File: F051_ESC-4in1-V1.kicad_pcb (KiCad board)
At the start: 4 copper layers, 46 x 40 mm, 249 parts, among them J1 Conn_01x02, J10 Conn_01x03, J11 Conn_01x03, J12 Conn_01x04, J13 Conn_01x03, J14 Conn_01x03, J15 Conn_01x04, J16 Conn_01x03, J17 Conn_01x03, J2 Conn_01x10, J3 Conn_01x04, J4 Conn_01x03, J5 Conn_01x04, J6 Conn_01x03, J7 Conn_01x03, J8 Conn_01x03, J9 Conn_01x04, Q1 TPHR8504PL, Q10 TPHR8504PL, Q11 TPHR8504PL, Q12 TPHR8504PL, Q13 TPHR8504PL, Q14 TPHR8504PL, Q15 TPHR8504PL, Q16 TPHR8504PL, Q17 TPHR8504PL, Q18 TPHR8504PL, Q19 TPHR8504PL, Q2 TPHR8504PL, Q20 TPHR8504PL, Q21 TPHR8504PL, Q22 TPHR8504PL, Q23 TPHR8504PL, Q24 TPHR8504PL, Q25 TPHR8504PL, Q26 TPHR8504PL, Q27 TPHR8504PL, Q28 TPHR8504PL, Q29 TPHR8504PL, Q3 TPHR8504PL, Q30 TPHR8504PL, Q4 TPHR8504PL, Q5 TPHR8504PL, Q6 TPHR8504PL, Q7 TPHR8504PL, Q8 TPHR8504PL, Q9 TPHR8504PL, U1 FD6288Q, U10 STM32F051K6Ux, U11 FD6288Q, U12 STM32F051K6Ux, U13 FD6288Q, U14 STM32F051K6Ux, U2 STM32F051K6Ux, U3 L78L12_SOT89, U4 LP2985-3.3, U5 INA139, U6 FD6288Q, U7 OPA340NA, U8 STM32F051K6Ux, U9 FD6288Q

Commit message: More design changes
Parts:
- removed C68, C74, C75, C76: 0.1uF, Capacitor_SMD:C_0402_1005Metric
- removed C69, C70, C71: 0.1uF, Capacitor_SMD:C_0603_1608Metric
- removed C72: 10nF, Capacitor_SMD:C_0402_1005Metric
- removed C73: 1uF, Capacitor_SMD:C_0402_1005Metric
- removed D13, D14, D15: 250V, Diode_SMD:D_SOD-523
- removed FB5: 100@100MHz, Inductor_SMD:L_0603_1608Metric
- removed J15: Conn_01x04, Connector_PinHeader_2.54mm:PinHeader_1x04_P2.54mm_Vertical
- removed J16: Conn_01x03, Connector_PinHeader_2.54mm:PinHeader_1x03_P2.54mm_Vertical
- removed J17: Conn_01x03, Connector_Wire:Conn_MotorPhase
- removed Q25, Q26, Q27, Q28, Q29, Q30: TPHR8504PL, Footprints:TPHR8504PL
- removed R72, R73, R74, R75, R76, R77: 10, Resistor_SMD:R_0402_1005Metric
- removed R78, R79, R80, R81, R83, R84: 10k, Resistor_SMD:R_0402_1005Metric
- removed R82, R85, R86, R87, R88: 1k, Resistor_SMD:R_0402_1005Metric
- removed U13: FD6288Q, Package_DFN_QFN:QFN-24-1EP_4x4mm_P0.5mm_EP2.7x2.7mm
- removed U14: STM32F051K6Ux, Package_DFN_QFN:QFN-32-1EP_5x5mm_P0.5mm_EP3.45x3.45mm
- C1, C32, C41: value 0.1uF -> 10nF
- C12, C34, C35, C43, C44: footprint Capacitor_SMD:C_0603_1608Metric -> Capacitor_SMD:C_0402_1005Metric
- C15, C38, C39, C40, C47, C48, C49: footprint Capacitor_SMD:C_0402_1005Metric -> Capacitor_SMD:C_0603_1608Metric
- C2: value 0.1uF -> 1uF
- C3, C36, C45: value 10nF -> 0.1uF
- C33, C42: value 0.1uF -> 1uF; footprint Capacitor_SMD:C_0603_1608Metric -> Capacitor_SMD:C_0402_1005Metric
- C37, C46, C6: value 1uF -> 0.1uF
- J10, J11, J12, J13, J14, J9, Q2, Q20: moved to B.Cu
- J4: footprint Connector_Wire:Conn_MotorPhase -> Connector_PinHeader_2.54mm:PinHeader_1x03_P2.54mm_Vertical
- J6: footprint Connector_PinHeader_2.54mm:PinHeader_1x03_P2.54mm_Vertical -> Connector_Wire:Conn_MotorPhase
- Q24, Q6: moved to F.Cu
- R10, R12, R38, R39, R40, R41, R43, R55, R56, R57, R58, R60, R7, R8, R9: value 10 -> 10k
- R11, R42, R59: value 10 -> 1k
- R14, R15, R17, R45, R46, R47, R62, R63, R64: value 10k -> 1k
- R18, R19, R49, R50, R66, R67: value 10k -> 10
- R20, R21, R23, R24, R51, R52, R53, R54, R68, R69, R70, R71: value 1k -> 10
- U1, U11, U9: value FD6288Q -> STM32F051K6Ux; footprint Package_DFN_QFN:QFN-24-1EP_4x4mm_P0.5mm_EP2.7x2.7mm -> Package_DFN_QFN:QFN-32-1EP_5x5mm_P0.5mm_EP3.45x3.45mm
- U10, U12, U2: value STM32F051K6Ux -> FD6288Q; footprint Package_DFN_QFN:QFN-32-1EP_5x5mm_P0.5mm_EP3.45x3.45mm -> Package_DFN_QFN:QFN-24-1EP_4x4mm_P0.5mm_EP2.7x2.7mm
- moved Q6 233.4 mm to (-8.07, 40.9), turned to 0 degrees
- moved Q18 231.0 mm to (-25.7, 28.0)
- moved Q13 221.5 mm to (-18.0, 27.2), turned to 180 degrees
- moved Q15 217.0 mm to (-18.0, 32.8), turned to 180 degrees
- moved Q17 213.0 mm to (-18.0, 38.4), turned to 180 degrees
- moved Q1 151.8 mm to (-0.31, 40.1), turned to 180 degrees
- moved Q3 146.2 mm to (-0.31, 45.7), turned to 180 degrees
- moved Q5 141.3 mm to (-0.31, 51.4), turned to 180 degrees
- moved Q24 115.9 mm to (148.8, 121.1), turned to 180 degrees
- moved R30 101.3 mm to (140.8, 53.3), turned to 0 degrees
- moved R31 101.3 mm to (140.8, 52.4), turned to 0 degrees
- moved R28 100.4 mm to (140.8, 56.3), turned to 0 degrees
- moved R29 100.1 mm to (140.8, 54.3), turned to 0 degrees
- moved R27 99.3 mm to (140.8, 57.3), turned to 0 degrees
- moved R35 98.9 mm to (140.8, 55.3), turned to 180 degrees
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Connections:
- C1 pad 1: +3V3 -> +3.3VA
- C11 pad 1: +12V -> /MCU 1/NRST
- C12 pad 1: /MOSFET Driver 1/VB2 -> +12V
- C12 pad 2: /MCU 1/PhaseB -> GND
- C14 pad 1: /MOSFET Driver 1/VB3 -> /MOSFET Driver 1/VB2
- C14 pad 2: /MCU 1/PhaseC -> /MCU 1/PhaseB
- C15 pad 1: /MCU 1/NRST -> /MOSFET Driver 1/VB3
- C15 pad 2: GND -> /MCU 1/PhaseC
- C2 pad 1: +3V3 -> +3.3VA
- C3 pad 1: +3.3VA -> +3V3
- C32 pad 1: +12V -> +3.3VA
- C33 pad 1: /MOSFET Driver 3/VB1 -> +3.3VA
- C33 pad 2: /MCU 3/PhaseA -> GND
- C34 pad 1: /MOSFET Driver 3/VB2 -> +3V3
- C34 pad 2: /MCU 3/PhaseB -> GND
- C35 pad 1: /MOSFET Driver 3/VB3 -> +3V3
- C35 pad 2: /MCU 3/PhaseC -> GND
- C36 pad 1: +3.3VA -> /MCU 3/NRST
- C37 pad 1: +3.3VA -> +12V
- C38 pad 1: +3V3 -> /MOSFET Driver 3/VB1
- C38 pad 2: GND -> /MCU 3/PhaseA
- C39 pad 1: +3V3 -> /MOSFET Driver 3/VB2
- C39 pad 2: GND -> /MCU 3/PhaseB
- C40 pad 1: /MCU 3/NRST -> /MOSFET Driver 3/VB3
- C40 pad 2: GND -> /MCU 3/PhaseC
- C41 pad 1: +12V -> +3.3VA
- C42 pad 1: /MOSFET Driver 4/VB1 -> +3.3VA
- C42 pad 2: /MCU 4/PhaseA -> GND
- C43 pad 1: /MOSFET Driver 4/VB2 -> +3V3
- C43 pad 2: /MCU 4/PhaseB -> GND
- C44 pad 1: /MOSFET Driver 4/VB3 -> +3V3
- C44 pad 2: /MCU 4/PhaseC -> GND
- C45 pad 1: +3.3VA -> /MCU 4/NRST
- C46 pad 1: +3.3VA -> +12V
- C47 pad 1: +3V3 -> /MOSFET Driver 4/VB1
- C47 pad 2: GND -> /MCU 4/PhaseA
- C48 pad 1: +3V3 -> /MOSFET Driver 4/VB2
- C48 pad 2: GND -> /MCU 4/PhaseB
- C49 pad 1: /MCU 4/NRST -> /MOSFET Driver 4/VB3
- C49 pad 2: GND -> /MCU 4/PhaseC
- C6 pad 1: +3.3VA -> +3V3
- D2 pad 1: /MOSFET Driver 1/VB2 -> /MOSFET Driver 1/VB1
- D3 pad 1: /MOSFET Driver 1/VB1 -> /MOSFET Driver 1/VB2
- J2 pad 10: /PWM_4 -> (no net)
- J2 pad 9: /PWM_3 -> (no net)
- J4 pad 1: /MCU 1/PhaseC -> /MCU 1/NRST
- J4 pad 2: /MCU 1/PhaseB -> /MCU 1/USART1_RX
- J4 pad 3: /MCU 1/PhaseA -> /MCU 1/USART1_TX
- J6 pad 1: /MCU 1/NRST -> /MCU 1/PhaseC
- J6 pad 2: /MCU 1/USART1_RX -> /MCU 1/PhaseB
- J6 pad 3: /MCU 1/USART1_TX -> /MCU 1/PhaseA
- R10 pad 1: Net-(Q4-Pad4) -> /MCU 1/SenseB
- R10 pad 2: /MOSFET Driver 1/LO2 -> /MCU 1/SenseCOM
- R11 pad 1: Net-(Q5-Pad4) -> Net-(R11-Pad1)
- R11 pad 2: /MOSFET Driver 1/HO3 -> /PWM_1
- R12 pad 1: Net-(Q6-Pad4) -> /MCU 1/SenseC
- R12 pad 2: /MOSFET Driver 1/LO3 -> /MCU 1/PhaseC
- R13 pad 1: /MCU 1/SenseA -> /MCU 1/SenseC
- R13 pad 2: /MCU 1/PhaseA -> /MCU 1/SenseCOM
- R14 pad 1: /MCU 1/SenseA -> GND
- R14 pad 2: /MCU 1/SenseCOM -> /MCU 1/SenseA
- R15 pad 1: /MCU 1/SenseB -> GND
- R15 pad 2: /MCU 1/PhaseB -> /MCU 1/SenseB
- R16 pad 2: /MCU 1/SenseA -> /MCU 1/SenseC
- R17 pad 1: /MCU 1/SenseB -> /MCU 1/BOOT0
- R17 pad 2: /MCU 1/SenseCOM -> GND
- R18 pad 1: /MCU 1/SenseC -> Net-(Q1-Pad4)
- R18 pad 2: /MCU 1/PhaseC -> /MOSFET Driver 1/HO1
- R19 pad 1: /MCU 1/SenseC -> Net-(Q2-Pad4)
- R19 pad 2: /MCU 1/SenseCOM -> /MOSFET Driver 1/LO1
- R20 pad 1: GND -> Net-(Q3-Pad4)
- R20 pad 2: /MCU 1/SenseB -> /MOSFET Driver 1/HO2
- R21 pad 1: GND -> Net-(Q4-Pad4)
- R21 pad 2: /MCU 1/SenseC -> /MOSFET Driver 1/LO2
- R23 pad 1: /MCU 1/BOOT0 -> Net-(Q5-Pad4)
- R23 pad 2: GND -> /MOSFET Driver 1/HO3
- R24 pad 1: Net-(R24-Pad1) -> Net-(Q6-Pad4)
- R24 pad 2: /PWM_1 -> /MOSFET Driver 1/LO3
- R38 pad 1: Net-(Q13-Pad4) -> /MCU 3/SenseA
- R38 pad 2: /MOSFET Driver 3/HO1 -> /MCU 3/PhaseA
- R39 pad 1: Net-(Q14-Pad4) -> /MCU 3/SenseA
- R39 pad 2: /MOSFET Driver 3/LO1 -> /MCU 3/SenseCOM
- R40 pad 1: Net-(Q15-Pad4) -> /MCU 3/SenseB
- R40 pad 2: /MOSFET Driver 3/HO2 -> /MCU 3/PhaseB
- R41 pad 1: Net-(Q16-Pad4) -> /MCU 3/SenseB
- R41 pad 2: /MOSFET Driver 3/LO2 -> /MCU 3/SenseCOM
- R42 pad 1: Net-(Q17-Pad4) -> Net-(R42-Pad1)
- R42 pad 2: /MOSFET Driver 3/HO3 -> /PWM_2
- R43 pad 1: Net-(Q18-Pad4) -> /MCU 3/SenseC
- R43 pad 2: /MOSFET Driver 3/LO3 -> /MCU 3/PhaseC
- R44 pad 1: /MCU 3/SenseA -> /MCU 3/SenseC
- R44 pad 2: /MCU 3/PhaseA -> /MCU 3/SenseCOM
- R45 pad 1: /MCU 3/SenseA -> GND
- R45 pad 2: /MCU 3/SenseCOM -> /MCU 3/SenseA
- R46 pad 1: /MCU 3/SenseB -> GND
- R46 pad 2: /MCU 3/PhaseB -> /MCU 3/SenseB
- R47 pad 1: /MCU 3/SenseB -> GND
- R47 pad 2: /MCU 3/SenseCOM -> /MCU 3/SenseC
- R48 pad 1: Net-(R48-Pad1) -> /MCU 3/BOOT0
- R48 pad 2: /PWM_3 -> GND
- R49 pad 1: /MCU 3/SenseC -> Net-(Q13-Pad4)
- R49 pad 2: /MCU 3/PhaseC -> /MOSFET Driver 3/HO1
- R50 pad 1: /MCU 3/SenseC -> Net-(Q14-Pad4)
- R50 pad 2: /MCU 3/SenseCOM -> /MOSFET Driver 3/LO1
- R51 pad 1: GND -> Net-(Q15-Pad4)
- R51 pad 2: /MCU 3/SenseA -> /MOSFET Driver 3/HO2
- R52 pad 1: GND -> Net-(Q16-Pad4)
- R52 pad 2: /MCU 3/SenseB -> /MOSFET Driver 3/LO2
- R53 pad 1: GND -> Net-(Q17-Pad4)
- R53 pad 2: /MCU 3/SenseC -> /MOSFET Driver 3/HO3
- R54 pad 1: /MCU 3/BOOT0 -> Net-(Q18-Pad4)
- R54 pad 2: GND -> /MOSFET Driver 3/LO3
- R55 pad 1: Net-(Q19-Pad4) -> /MCU 4/SenseA
- R55 pad 2: /MOSFET Driver 4/HO1 -> /MCU 4/PhaseA
- R56 pad 1: Net-(Q20-Pad4) -> /MCU 4/SenseA
- R56 pad 2: /MOSFET Driver 4/LO1 -> /MCU 4/SenseCOM
- R57 pad 1: Net-(Q21-Pad4) -> /MCU 4/SenseB
- R57 pad 2: /MOSFET Driver 4/HO2 -> /MCU 4/PhaseB
- R58 pad 1: Net-(Q22-Pad4) -> /MCU 4/SenseB
- R58 pad 2: /MOSFET Driver 4/LO2 -> /MCU 4/SenseCOM
- R59 pad 1: Net-(Q23-Pad4) -> Net-(R59-Pad1)
- R59 pad 2: /MOSFET Driver 4/HO3 -> /PWM_2
- R60 pad 1: Net-(Q24-Pad4) -> /MCU 4/SenseC
- R60 pad 2: /MOSFET Driver 4/LO3 -> /MCU 4/PhaseC
- R61 pad 1: /MCU 4/SenseA -> /MCU 4/SenseC
- R61 pad 2: /MCU 4/PhaseA -> /MCU 4/SenseCOM
- R62 pad 1: /MCU 4/SenseA -> GND
- R62 pad 2: /MCU 4/SenseCOM -> /MCU 4/SenseA
- R63 pad 1: /MCU 4/SenseB -> GND
- R63 pad 2: /MCU 4/PhaseB -> /MCU 4/SenseB
- R64 pad 1: /MCU 4/SenseB -> GND
- R64 pad 2: /MCU 4/SenseCOM -> /MCU 4/SenseC
- R65 pad 1: Net-(R65-Pad1) -> /MCU 4/BOOT0
- R65 pad 2: /PWM_4 -> GND
- R66 pad 1: /MCU 4/SenseC -> Net-(Q19-Pad4)
- R66 pad 2: /MCU 4/PhaseC -> /MOSFET Driver 4/HO1
- R67 pad 1: /MCU 4/SenseC -> Net-(Q20-Pad4)
- R67 pad 2: /MCU 4/SenseCOM -> /MOSFET Driver 4/LO1
- R68 pad 1: GND -> Net-(Q21-Pad4)
- R68 pad 2: /MCU 4/SenseA -> /MOSFET Driver 4/HO2
- R69 pad 1: GND -> Net-(Q22-Pad4)
- R69 pad 2: /MCU 4/SenseB -> /MOSFET Driver 4/LO2
- R7 pad 1: Net-(Q1-Pad4) -> /MCU 1/SenseA
- R7 pad 2: /MOSFET Driver 1/HO1 -> /MCU 1/PhaseA
- R70 pad 1: GND -> Net-(Q23-Pad4)
- R70 pad 2: /MCU 4/SenseC -> /MOSFET Driver 4/HO3
- R71 pad 1: /MCU 4/BOOT0 -> Net-(Q24-Pad4)
- R71 pad 2: GND -> /MOSFET Driver 4/LO3
- R8 pad 1: Net-(Q2-Pad4) -> /MCU 1/SenseA
- R8 pad 2: /MOSFET Driver 1/LO1 -> /MCU 1/SenseCOM
- R9 pad 1: Net-(Q3-Pad4) -> /MCU 1/SenseB
- R9 pad 2: /MOSFET Driver 1/HO2 -> /MCU 1/PhaseB
- U1 pad 1: /MCU 1/LIN1 -> +3V3
- U1 pad 10: /MOSFET Driver 1/LO2 -> /MCU 1/SenseB
- U1 pad 11: /MOSFET Driver 1/LO1 -> /MCU 1/SenseA
- U1 pad 12: /MCU 1/PhaseC -> (no net)
- U1 pad 13: /MOSFET Driver 1/HO3 -> /MCU 1/LIN3
- U1 pad 14: /MOSFET Driver 1/VB3 -> /MCU 1/LIN2
- U1 pad 15: /MCU 1/PhaseB -> /MCU 1/LIN1
- U1 pad 16: /MOSFET Driver 1/HO2 -> (no net)
- U1 pad 17: /MOSFET Driver 1/VB2 -> +3V3
- U1 pad 18: /MCU 1/PhaseA -> /MCU 1/HIN1
- U1 pad 19: /MOSFET Driver 1/HO1 -> /MCU 1/HIN2
- U1 pad 2: /MCU 1/LIN2 -> (no net)
- U1 pad 20: /MOSFET Driver 1/VB1 -> /MOSFET Driver 1/HIN1
- U1 pad 22: /MOSFET Driver 1/HIN1 -> (no net)
- U1 pad 23: /MCU 1/HIN2 -> /MCU 1/SWDIO
- U1 pad 24: /MCU 1/HIN1 -> /MCU 1/SWCLK
- U1 pad 25: GND -> (no net)
- U1 pad 3: /MCU 1/LIN3 -> (no net)
- U1 pad 4: +12V -> /MCU 1/NRST
- U1 pad 5: (no net) -> +3.3VA
- U1 pad 6: GND -> /MCU 1/SenseC
- U1 pad 7: (no net) -> /MCU 1/SenseCOM
- U1 pad 8: (no net) -> Net-(R11-Pad1)
- U1 pad 9: /MOSFET Driver 1/LO3 -> (no net)
- U10 pad 1: +3V3 -> /MCU 3/LIN1
- U10 pad 10: /MCU 3/SenseB -> /MOSFET Driver 3/LO2
- U10 pad 11: /MCU 3/SenseA -> /MOSFET Driver 3/LO1
- U10 pad 12: (no net) -> /MCU 3/PhaseC
- U10 pad 13: /MCU 3/LIN3 -> /MOSFET Driver 3/HO3
- U10 pad 14: /MCU 3/LIN2 -> /MOSFET Driver 3/VB3
- U10 pad 15: /MCU 3/LIN1 -> /MCU 3/PhaseB
- U10 pad 16: (no net) -> /MOSFET Driver 3/HO2
- U10 pad 17: +3V3 -> /MOSFET Driver 3/VB2
- U10 pad 18: /MCU 3/HIN1 -> /MCU 3/PhaseA
- U10 pad 19: /MCU 3/HIN2 -> /MOSFET Driver 3/HO1
- U10 pad 2: (no net) -> /MCU 3/LIN2
- U10 pad 20: /MOSFET Driver 3/HIN1 -> /MOSFET Driver 3/VB1
- U10 pad 22: (no net) -> /MOSFET Driver 3/HIN1
- U10 pad 23: /MCU 3/SWDIO -> /MCU 3/HIN2
- U10 pad 24: /MCU 3/SWCLK -> /MCU 3/HIN1
- U10 pad 25: (no net) -> GND
- U10 pad 3: (no net) -> /MCU 3/LIN3
- U10 pad 4: /MCU 3/NRST -> +12V
- U10 pad 5: +3.3VA -> (no net)
- U10 pad 6: /MCU 3/SenseC -> GND
- U10 pad 7: /MCU 3/SenseCOM -> (no net)
- U10 pad 8: Net-(R48-Pad1) -> (no net)
- U10 pad 9: (no net) -> /MOSFET Driver 3/LO3
- U11 pad 1: /MCU 4/LIN1 -> +3V3
- U11 pad 10: /MOSFET Driver 4/LO2 -> /MCU 4/SenseB
- U11 pad 11: /MOSFET Driver 4/LO1 -> /MCU 4/SenseA
- U11 pad 12: /MCU 4/PhaseC -> (no net)
- U11 pad 13: /MOSFET Driver 4/HO3 -> /MCU 4/LIN3
- U11 pad 14: /MOSFET Driver 4/VB3 -> /MCU 4/LIN2
- U11 pad 15: /MCU 4/PhaseB -> /MCU 4/LIN1
- U11 pad 16: /MOSFET Driver 4/HO2 -> (no net)
- U11 pad 17: /MOSFET Driver 4/VB2 -> +3V3
- U11 pad 18: /MCU 4/PhaseA -> /MCU 4/HIN1
- U11 pad 19: /MOSFET Driver 4/HO1 -> /MCU 4/HIN2
- U11 pad 2: /MCU 4/LIN2 -> (no net)
- U11 pad 20: /MOSFET Driver 4/VB1 -> /MOSFET Driver 4/HIN1
- U11 pad 22: /MOSFET Driver 4/HIN1 -> (no net)
- U11 pad 23: /MCU 4/HIN2 -> /MCU 4/SWDIO
- U11 pad 24: /MCU 4/HIN1 -> /MCU 4/SWCLK
- U11 pad 25: GND -> (no net)
- U11 pad 3: /MCU 4/LIN3 -> (no net)
- U11 pad 4: +12V -> /MCU 4/NRST
- U11 pad 5: (no net) -> +3.3VA
- U11 pad 6: GND -> /MCU 4/SenseC
- U11 pad 7: (no net) -> /MCU 4/SenseCOM
- U11 pad 8: (no net) -> Net-(R59-Pad1)
- U11 pad 9: /MOSFET Driver 4/LO3 -> (no net)
- U12 pad 1: +3V3 -> /MCU 4/LIN1
- U12 pad 10: /MCU 4/SenseB -> /MOSFET Driver 4/LO2
- U12 pad 11: /MCU 4/SenseA -> /MOSFET Driver 4/LO1
- U12 pad 12: (no net) -> /MCU 4/PhaseC
- U12 pad 13: /MCU 4/LIN3 -> /MOSFET Driver 4/HO3
- U12 pad 14: /MCU 4/LIN2 -> /MOSFET Driver 4/VB3
- U12 pad 15: /MCU 4/LIN1 -> /MCU 4/PhaseB
- U12 pad 16: (no net) -> /MOSFET Driver 4/HO2
- U12 pad 17: +3V3 -> /MOSFET Driver 4/VB2
- U12 pad 18: /MCU 4/HIN1 -> /MCU 4/PhaseA
- U12 pad 19: /MCU 4/HIN2 -> /MOSFET Driver 4/HO1
- U12 pad 2: (no net) -> /MCU 4/LIN2
- U12 pad 20: /MOSFET Driver 4/HIN1 -> /MOSFET Driver 4/VB1
- U12 pad 22: (no net) -> /MOSFET Driver 4/HIN1
- U12 pad 23: /MCU 4/SWDIO -> /MCU 4/HIN2
- U12 pad 24: /MCU 4/SWCLK -> /MCU 4/HIN1
- U12 pad 25: (no net) -> GND
- U12 pad 3: (no net) -> /MCU 4/LIN3
- U12 pad 4: /MCU 4/NRST -> +12V
- U12 pad 5: +3.3VA -> (no net)
- U12 pad 6: /MCU 4/SenseC -> GND
- U12 pad 7: /MCU 4/SenseCOM -> (no net)
- U12 pad 8: Net-(R65-Pad1) -> (no net)
- U12 pad 9: (no net) -> /MOSFET Driver 4/LO3
- U2 pad 1: +3V3 -> /MCU 1/LIN1
- U2 pad 10: /MCU 1/SenseB -> /MOSFET Driver 1/LO2
- U2 pad 11: /MCU 1/SenseA -> /MOSFET Driver 1/LO1
- U2 pad 12: (no net) -> /MCU 1/PhaseC
- U2 pad 13: /MCU 1/LIN3 -> /MOSFET Driver 1/HO3
- U2 pad 14: /MCU 1/LIN2 -> /MOSFET Driver 1/VB3
- U2 pad 15: /MCU 1/LIN1 -> /MCU 1/PhaseB
- U2 pad 16: (no net) -> /MOSFET Driver 1/HO2
- U2 pad 17: +3V3 -> /MOSFET Driver 1/VB2
- U2 pad 18: /MCU 1/HIN1 -> /MCU 1/PhaseA
- U2 pad 19: /MCU 1/HIN2 -> /MOSFET Driver 1/HO1
- U2 pad 2: (no net) -> /MCU 1/LIN2
- U2 pad 20: /MOSFET Driver 1/HIN1 -> /MOSFET Driver 1/VB1
- U2 pad 22: (no net) -> /MOSFET Driver 1/HIN1
- U2 pad 23: /MCU 1/SWDIO -> /MCU 1/HIN2
- U2 pad 24: /MCU 1/SWCLK -> /MCU 1/HIN1
- U2 pad 25: (no net) -> GND
- U2 pad 3: (no net) -> /MCU 1/LIN3
- U2 pad 4: /MCU 1/NRST -> +12V
- U2 pad 5: +3.3VA -> (no net)
- U2 pad 6: /MCU 1/SenseC -> GND
- U2 pad 7: /MCU 1/SenseCOM -> (no net)
- U2 pad 8: Net-(R24-Pad1) -> (no net)
- U2 pad 9: (no net) -> /MOSFET Driver 1/LO3
- U9 pad 1: /MCU 3/LIN1 -> +3V3
- U9 pad 10: /MOSFET Driver 3/LO2 -> /MCU 3/SenseB
- U9 pad 11: /MOSFET Driver 3/LO1 -> /MCU 3/SenseA
- U9 pad 12: /MCU 3/PhaseC -> (no net)
- U9 pad 13: /MOSFET Driver 3/HO3 -> /MCU 3/LIN3
- U9 pad 14: /MOSFET Driver 3/VB3 -> /MCU 3/LIN2
- U9 pad 15: /MCU 3/PhaseB -> /MCU 3/LIN1
- U9 pad 16: /MOSFET Driver 3/HO2 -> (no net)
- U9 pad 17: /MOSFET Driver 3/VB2 -> +3V3
- U9 pad 18: /MCU 3/PhaseA -> /MCU 3/HIN1
- U9 pad 19: /MOSFET Driver 3/HO1 -> /MCU 3/HIN2
- U9 pad 2: /MCU 3/LIN2 -> (no net)
- U9 pad 20: /MOSFET Driver 3/VB1 -> /MOSFET Driver 3/HIN1
- U9 pad 22: /MOSFET Driver 3/HIN1 -> (no net)
- U9 pad 23: /MCU 3/HIN2 -> /MCU 3/SWDIO
- U9 pad 24: /MCU 3/HIN1 -> /MCU 3/SWCLK
- U9 pad 25: GND -> (no net)
- U9 pad 3: /MCU 3/LIN3 -> (no net)
- U9 pad 4: +12V -> /MCU 3/NRST
- U9 pad 5: (no net) -> +3.3VA
- U9 pad 6: GND -> /MCU 3/SenseC
- U9 pad 7: (no net) -> /MCU 3/SenseCOM
- U9 pad 8: (no net) -> Net-(R42-Pad1)
- U9 pad 9: /MOSFET Driver 3/LO3 -> (no net)
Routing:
- net GND: track 33.4 -> 3.56 mm, vias 119 -> 75
- net +12V: track 25.0 -> 9.68 mm, vias 16 -> 0
- net +3.3VA: track 23.3 -> 12.2 mm
- net /MCU Test/SenseCOM: track 9.59 -> 0.00 mm
- net /MOSFET Driver 4/HIN1: track 9.12 -> 1.60 mm
- net /MOSFET Driver 1/HIN1: track 9.12 -> 1.60 mm
- net /MOSFET Driver 2/HIN1: track 9.12 -> 1.60 mm
- net /MOSFET Driver 3/HIN1: track 9.12 -> 1.60 mm
- net /MCU Test/LIN3: track 7.44 -> 0.00 mm
- net /MCU Test/LIN2: track 6.51 -> 0.00 mm
- net /MCU 3/HIN2: track 8.07 -> 1.60 mm
- net /MCU 4/HIN2: track 8.07 -> 1.60 mm
- net /MCU 1/HIN2: track 8.07 -> 1.60 mm
- net /MCU 2/HIN2: track 8.07 -> 1.60 mm
- net /MOSFET Driver Test/VB1: track 6.46 -> 0.00 mm
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
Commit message: Circuit added to board
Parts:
- Q12, Q18, Q24, Q6: moved to B.Cu
- moved Q6 264.2 mm to (254.2, 72.8)
- moved Q18 234.9 mm to (206.0, 66.3)
- moved Q13 222.4 mm to (187.7, 112.0)
- moved Q15 222.4 mm to (187.7, 117.6)
- moved Q17 222.4 mm to (187.7, 123.2)
- moved Q1 181.3 mm to (166.4, 111.3)
- moved Q3 181.3 mm to (166.4, 116.9)
- moved Q5 181.3 mm to (166.4, 122.6)
- moved R18 135.8 mm to (249.6, 74.4), turned to 270 degrees
- moved R20 135.5 mm to (249.6, 71.5), turned to 270 degrees
- moved R23 135.3 mm to (249.6, 68.5), turned to 270 degrees
- moved C13 133.1 mm to (248.0, 75.9), turned to 180 degrees
- moved D2 133.0 mm to (247.8, 77.4), turned to 180 degrees
- moved R17 132.8 mm to (247.0, 81.6), turned to 270 degrees
- moved C3 132.8 mm to (246.6, 83.5), turned to 270 degrees
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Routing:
- net +3.3VA: track 12.2 -> 12.8 mm

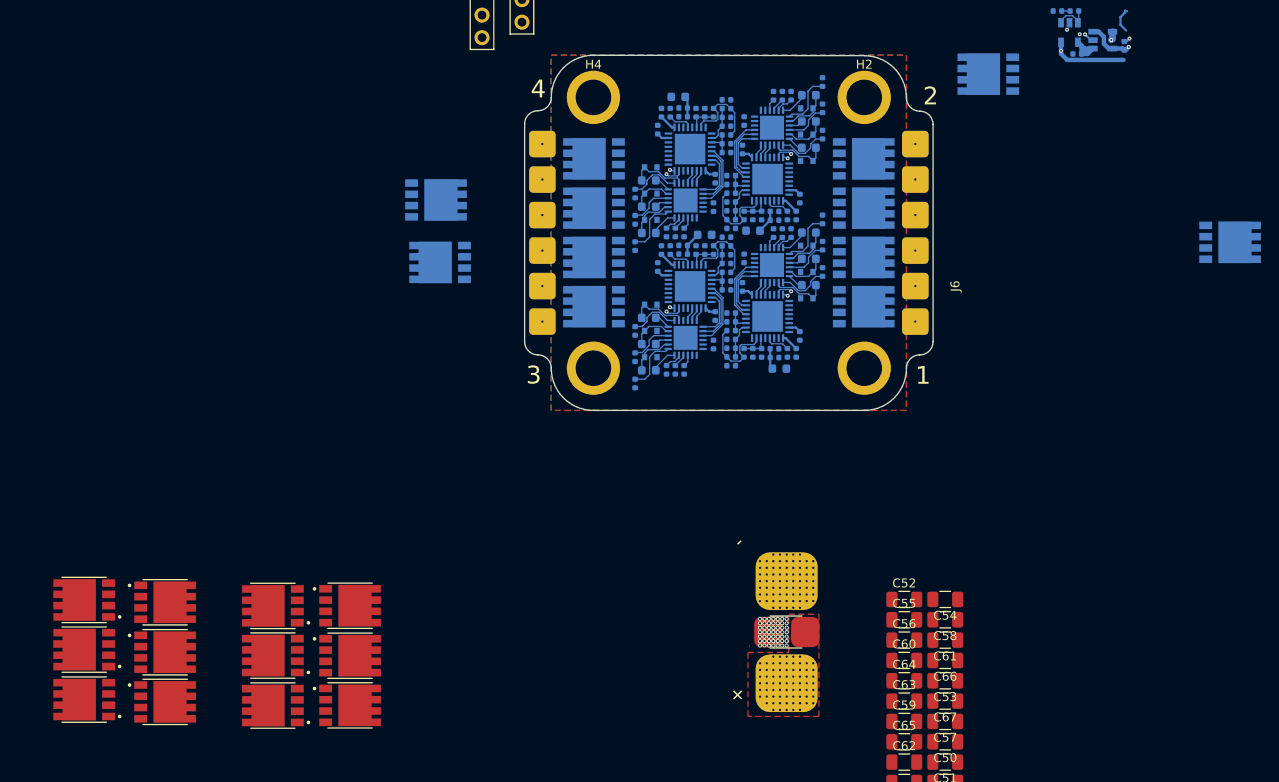
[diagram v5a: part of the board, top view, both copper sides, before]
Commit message: Finalized back layer and added FETs to front layer
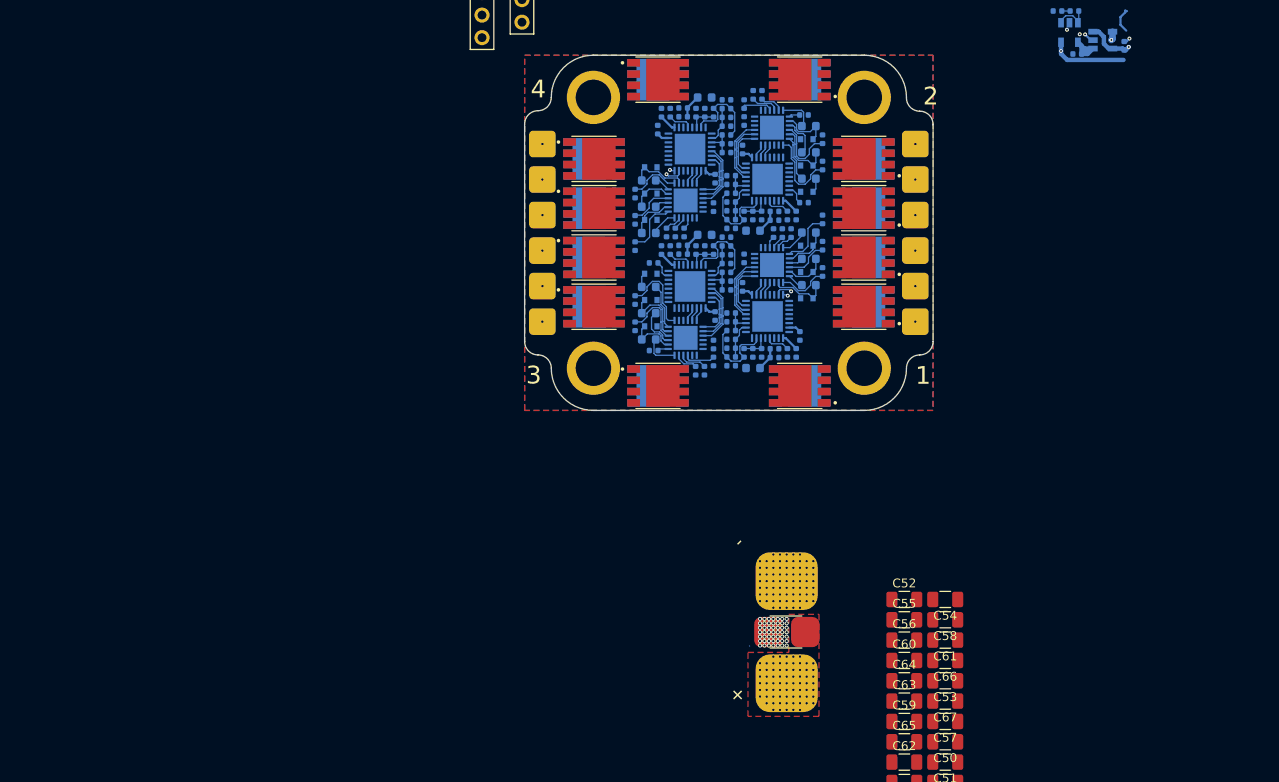
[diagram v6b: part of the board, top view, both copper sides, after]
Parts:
- moved Q5 100.9 mm to (254.2, 72.8)
- moved Q7 96.3 mm to (254.2, 67.2), turned to 180 degrees
- moved Q9 96.3 mm to (254.2, 61.7), turned to 180 degrees
- moved Q3 95.9 mm to (254.2, 78.3)
- moved Q11 92.6 mm to (247.0, 52.7), turned to 180 degrees
- moved Q1 84.1 mm to (247.0, 87.2)
- moved Q19 78.5 mm to (231.0, 52.8)
- moved Q21 62.3 mm to (223.8, 61.7)
- moved Q17 56.4 mm to (231.0, 87.2), turned to 0 degrees
- moved Q15 53.4 mm to (223.8, 78.3), turned to 0 degrees
- moved Q13 53.4 mm to (223.8, 72.8), turned to 0 degrees
- moved Q23 52.5 mm to (223.8, 67.2)
- moved Q2 51.1 mm to (247.0, 87.2)
- moved Q18 32.6 mm to (231.0, 87.2), turned to 180 degrees
- moved Q20 32.0 mm to (231.0, 52.8)
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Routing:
- net /MOSFET Driver 2/HO3: track 6.31 -> 1.23 mm
- net /MOSFET Driver 3/HO3: track 6.31 -> 1.23 mm
- net /MOSFET Driver 3/VB1: track 6.46 -> 1.61 mm
- net /MOSFET Driver 2/VB1: track 6.46 -> 1.61 mm
- net /MCU 2/PhaseA: track 1.82 -> 5.46 mm
- net /MOSFET Driver 3/HO1: track 5.74 -> 9.14 mm
- net /MOSFET Driver 2/HO1: track 5.74 -> 9.13 mm
- net /MCU 3/PhaseA: track 1.82 -> 5.07 mm
- net /MCU 3/PhaseB: track 1.59 -> 4.59 mm
- net /MCU 2/PhaseB: track 1.59 -> 4.49 mm
- net /MOSFET Driver 3/VB2: track 4.70 -> 7.54 mm
- net /MOSFET Driver 2/HO2: track 4.89 -> 7.49 mm
- net /MOSFET Driver 3/HO2: track 4.89 -> 7.32 mm
- net /MOSFET Driver 2/VB2: track 4.70 -> 7.08 mm
- net /MOSFET Driver 2/LO3: track 1.33 -> 3.57 mm
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
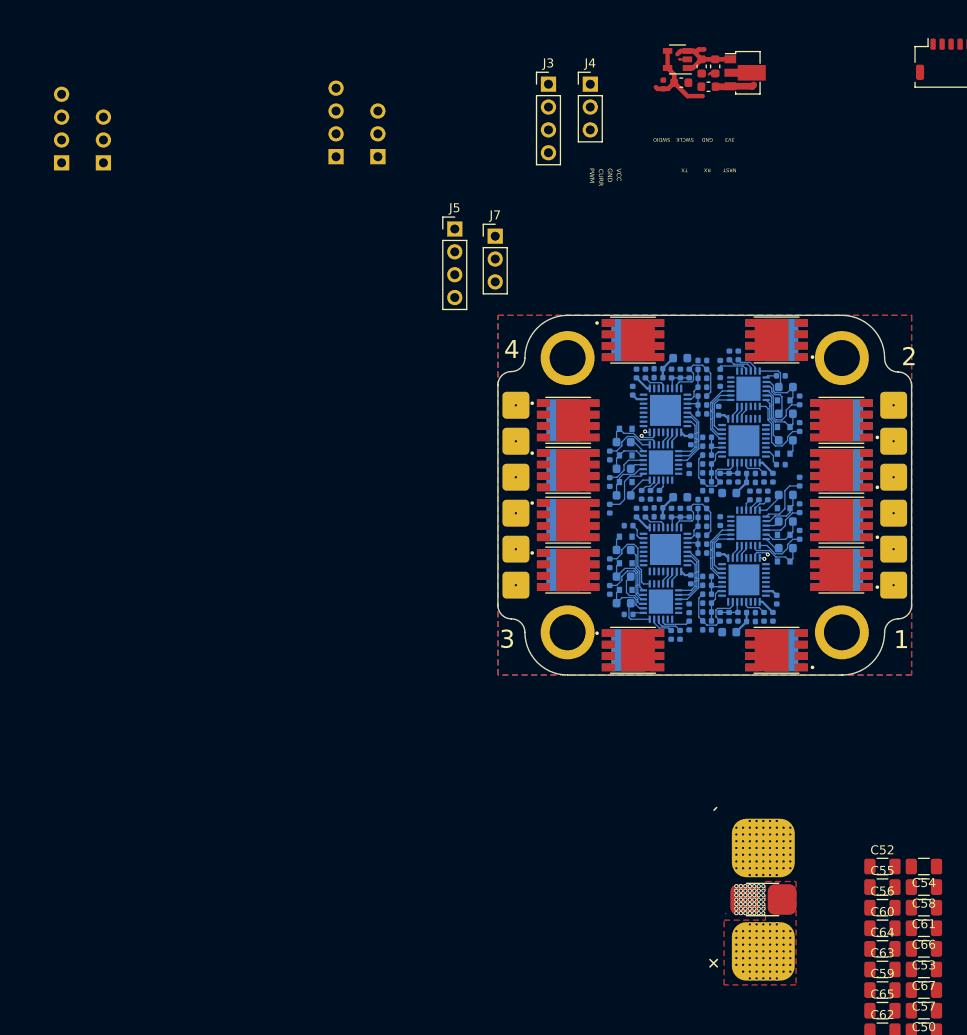
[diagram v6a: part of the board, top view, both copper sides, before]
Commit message: Added pads for battery and debugging
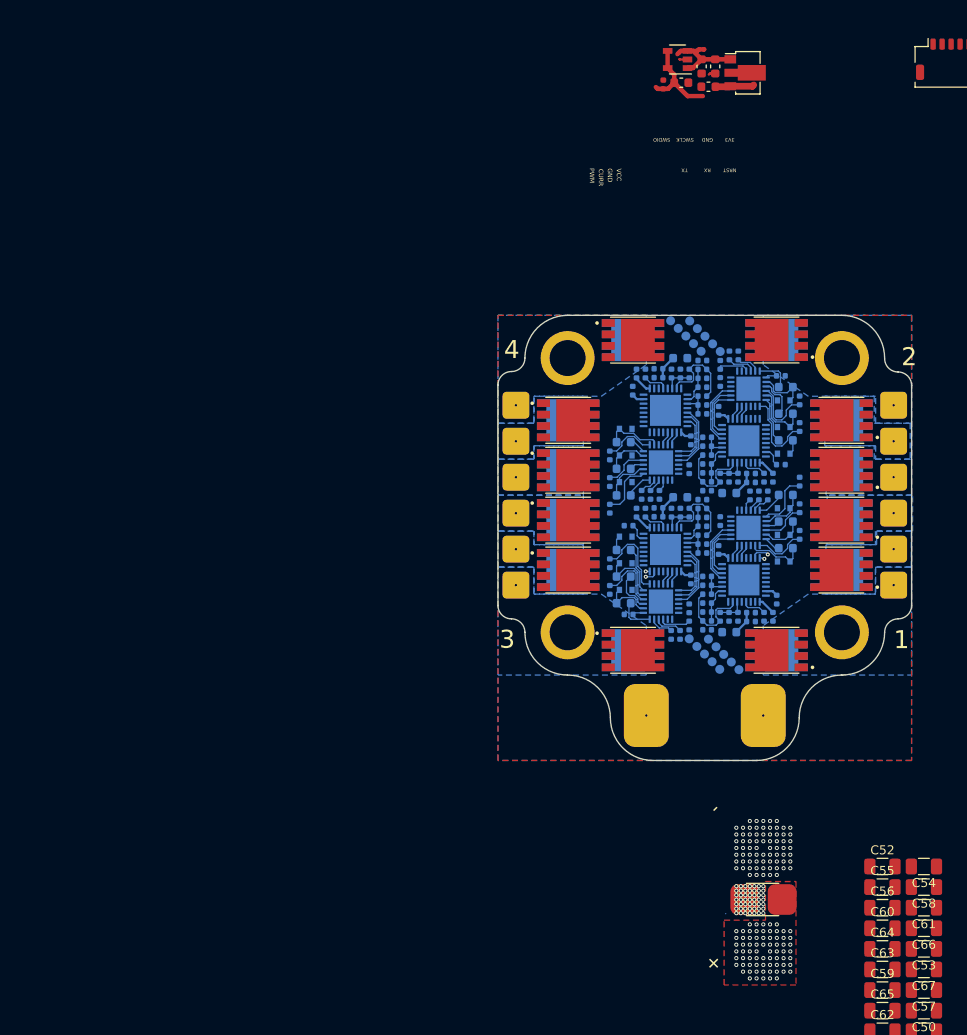
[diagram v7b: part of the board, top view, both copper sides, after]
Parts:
- removed J10, J13: Conn_01x03, Connector_PinHeader_2.54mm:PinHeader_1x03_P2.54mm_Vertical
- removed J12, J9: Conn_01x04, Connector_PinHeader_2.54mm:PinHeader_1x04_P2.54mm_Vertical
- J1: footprint Connector_Wire:Conn_PowerPad -> Connector_Wire:Conn_PowerPad_4in1
- J3, J5: value Conn_01x04 -> Conn_01x05; footprint Connector_PinHeader_2.54mm:PinHeader_1x04_P2.54mm_Vertical -> Connector_Wire:Conn_Debug; moved to B.Cu
- J4, J7: value Conn_01x03 -> Conn_01x05; footprint Connector_PinHeader_2.54mm:PinHeader_1x03_P2.54mm_Vertical -> Connector_Wire:Conn_Debug; moved to B.Cu
- moved J3 66.3 mm to (241.1, 87.7), turned to 135 degrees
- moved J4 64.6 mm to (239.0, 87.7), turned to 135 degrees
- moved J5 30.3 mm to (239.0, 52.3), turned to 135 degrees
- moved J7 23.9 mm to (236.9, 52.3), turned to 135 degrees
- moved J1 21.3 mm to (239.0, 94.5), turned to 180 degrees
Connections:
- J2 pad 10: (no net) -> /PWM_4
- J2 pad 9: (no net) -> /PWM_3
- J3 pad 1: +3V3 -> /MCU 1/SWCLK
- J3 pad 2: GND -> /MCU 1/SWDIO
- J3 pad 3: /MCU 1/SWCLK -> /MCU 1/NRST
- J3 pad 4: /MCU 1/SWDIO -> /MCU 1/USART1_RX
- J4 pad 1: /MCU 1/NRST -> /MCU 3/SWCLK
- J4 pad 2: /MCU 1/USART1_RX -> /MCU 3/SWDIO
- J4 pad 3: /MCU 1/USART1_TX -> /MCU 3/NRST
- J5 pad 1: +3V3 -> /MCU 2/SWCLK
- J5 pad 2: GND -> /MCU 2/SWDIO
- J5 pad 3: /MCU 2/SWCLK -> /MCU 2/NRST
- J5 pad 4: /MCU 2/SWDIO -> /MCU 2/USART1_RX
- J7 pad 1: /MCU 2/NRST -> /MCU 4/SWCLK
- J7 pad 2: /MCU 2/USART1_RX -> /MCU 4/SWDIO
- J7 pad 3: /MCU 2/USART1_TX -> /MCU 4/NRST
- R42 pad 2: /PWM_2 -> /PWM_3
- R59 pad 2: /PWM_2 -> /PWM_4
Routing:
- net /MCU 4/SWDIO: track 1.98 -> 0.00 mm, vias 1 -> 0
- net /MCU 3/SWDIO: track 0.00 -> 1.44 mm, vias 0 -> 1
- net /MCU 4/SWCLK: track 0.56 -> 0.00 mm, vias 1 -> 0
- net /MCU 3/SWCLK: track 0.00 -> 0.45 mm, vias 0 -> 1
- added copper zone on B.Cu, net /MCU 1/PhaseA
- added copper zone on B.Cu, net /MCU 1/PhaseB
- added copper zone on B.Cu, net /MCU 1/PhaseC
- added copper zone on B.Cu, net /MCU 2/PhaseA
- added copper zone on B.Cu, net /MCU 2/PhaseB
- added copper zone on B.Cu, net /MCU 2/PhaseC
- added copper zone on B.Cu, net /MCU 3/PhaseA
- added copper zone on B.Cu, net /MCU 3/PhaseB
- added copper zone on B.Cu, net /MCU 3/PhaseC
- added copper zone on B.Cu, net /MCU 4/PhaseA
- added copper zone on B.Cu, net /MCU 4/PhaseB
- added copper zone on B.Cu, net /MCU 4/PhaseC
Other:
- board size 46 x 40 mm -> 46 x 49.5 mm
